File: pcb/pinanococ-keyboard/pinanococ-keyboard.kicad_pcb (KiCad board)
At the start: 2 copper layers, 146.5 x 137.2 mm, 70 parts, among them J1 AudioJack4, SW1 SW_Push, SW10 SW_Push, SW11 SW_Push, SW12 SW_Push, SW14 SW_Push, SW15 SW_Push, SW16 SW_Push, SW17 SW_Push, SW18 SW_Push, SW2 SW_Push, SW20 SW_Push_Dual_x2, SW21 SW_Push, SW22 SW_Push, SW23 SW_Push, SW24 SW_Push, SW26 SW_Push_Dual_x2, SW27 SW_Push, SW28 SW_Push, SW29 SW_Push, SW3 SW_Push, SW30 SW_Push, SW32 SW_Push_Dual_x2, SW33 SW_Push, SW34 SW_Push, SW35 SW_Push, SW36 SW_Push, SW37 SW_Push, SW38 Rotary_Encoder_Switch, SW4 SW_Push, SW5 SW_Push, SW6 SW_Push, SW8 SW_Push, SW9 SW_Push, U1 Pico

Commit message: pcb component layout
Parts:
- added D13: D_ALT, Diode_THT:D_DO-34_SOD68_P7.62mm_Horizontal, F.Cu at (86.2, 134.2)
- SW14: value SW_Push -> SW_Push_Dual_x2; footprint keyswitches:SW_PG1350 -> keyswitches:SW_PG1350_double_rotate
- moved SW14 13.2 mm to (78.0, 124.5)
- moved D14 12.1 mm to (86.2, 124.1)
- moved SW38 5.86 mm to (128.5, 118.8)
- moved U1 5.85 mm to (136.0, 73.0)
- moved e1 5.48 mm to (139.8, 102.0)
- moved D1 5.45 mm to (33.0, 131.2)
- moved D2 5.09 mm to (51.0, 131.1)
- moved D8 5.09 mm to (69.0, 131.1)
- moved D26 4.99 mm to (134.1, 141.2)
- moved D32 4.96 mm to (141.1, 146.6)
- moved SW1 4.70 mm to (24.0, 133.0)
- moved SW2 4.70 mm to (42.0, 133.0)
- moved SW8 4.70 mm to (60.0, 133.0)
- moved SW32 4.40 mm to (146.6, 152.9)
- moved D20 4.33 mm to (111.2, 129.4)
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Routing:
- net ROW_2: track 214.2 -> 0.00 mm
- net COL_0: track 172.7 -> 0.00 mm
- net ROW_3: track 167.2 -> 0.00 mm
- net COL_1: track 160.6 -> 0.00 mm
- net ROW_5: track 142.8 -> 0.00 mm
- net ROW_4: track 141.7 -> 0.00 mm
- net COL_2: track 134.6 -> 0.00 mm
- net COL_3: track 115.0 -> 0.00 mm
- net COL_4: track 101.4 -> 0.00 mm
- net VBUS: track 70.1 -> 0.00 mm
- net COL_5: track 59.7 -> 0.00 mm
- net GND: track 52.9 -> 0.00 mm
- net +3V3: track 49.0 -> 0.00 mm
- net Reset: track 47.8 -> 0.00 mm
- net ROT_B: track 39.6 -> 0.00 mm
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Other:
- board size 146.5 x 137.2 mm -> 146 x 140.8 mm
- net class Default: clearance 0.2 -> 0.254
- rule trace_clearance: 0.2 -> 0.254

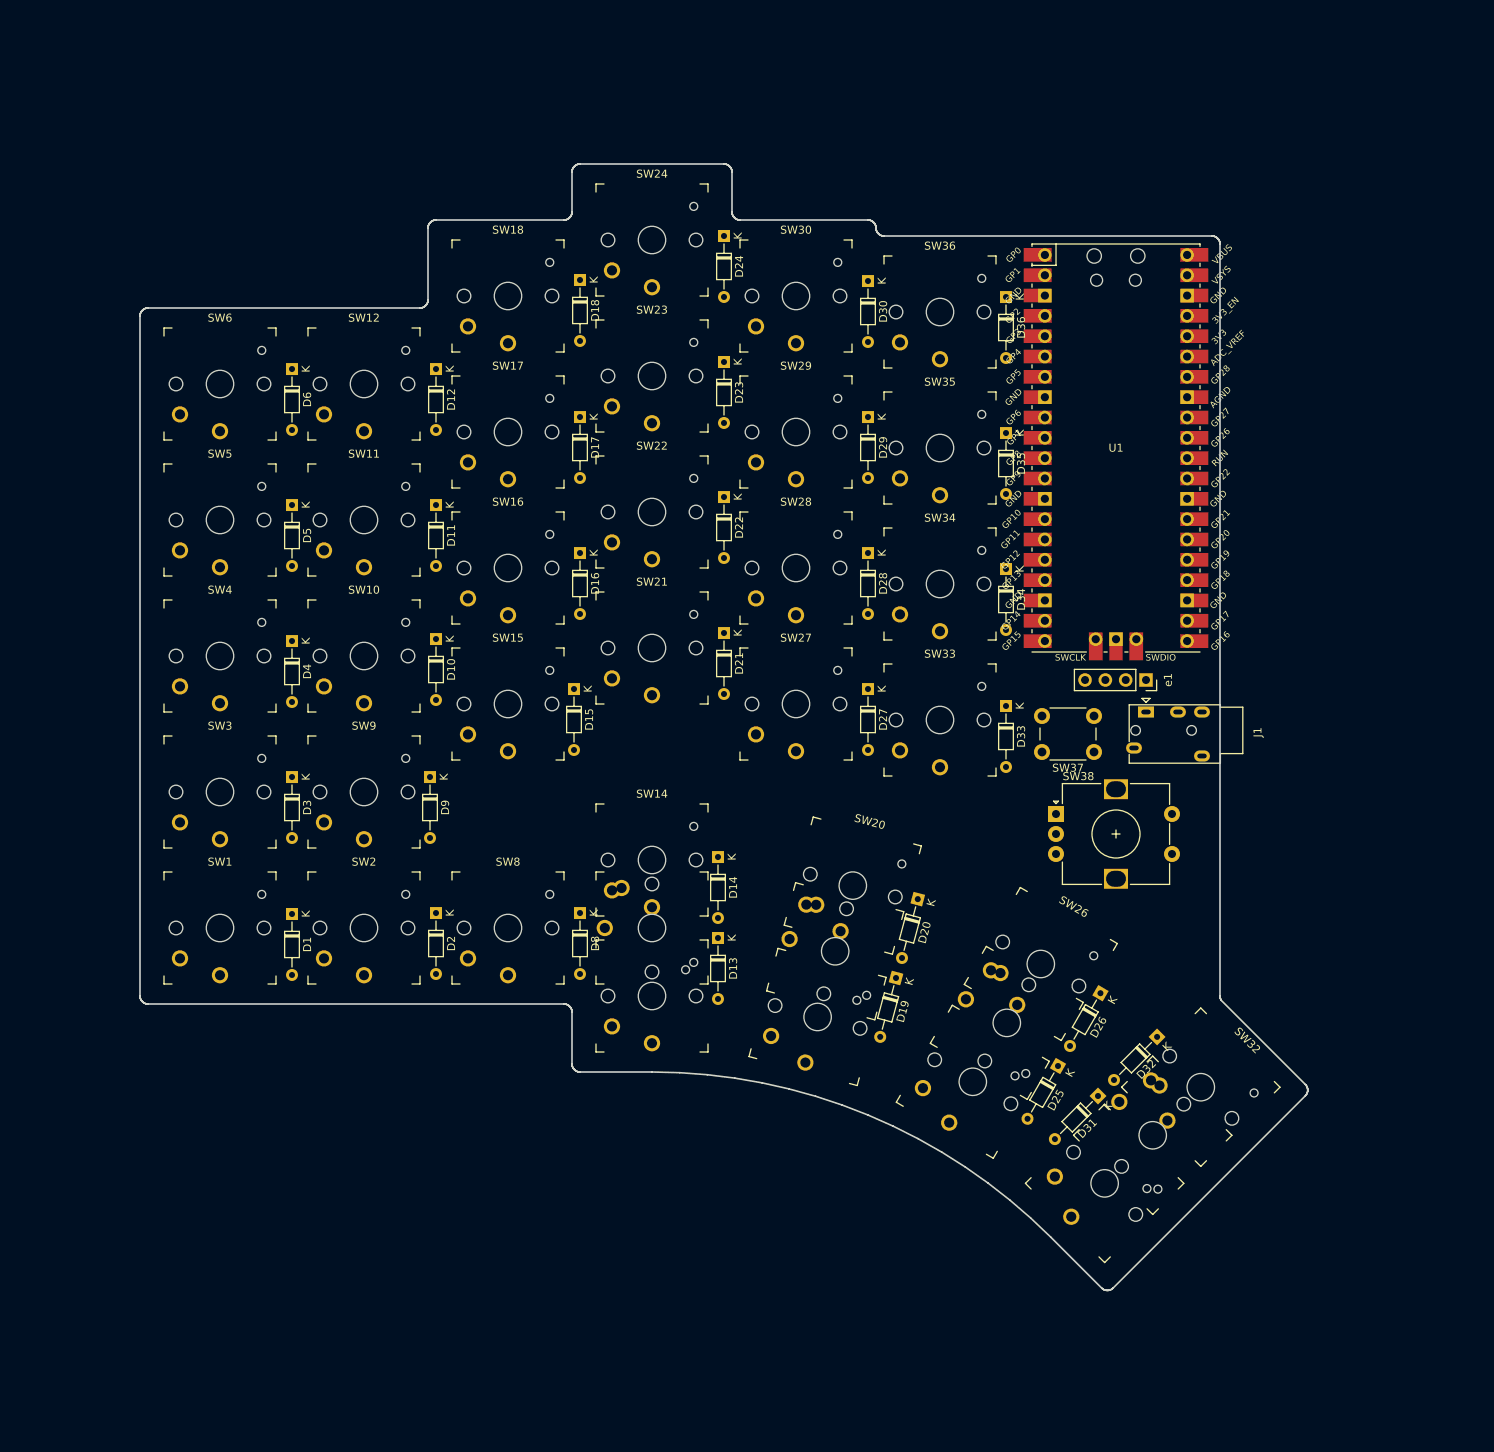
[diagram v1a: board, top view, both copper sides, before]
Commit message: inital pcb layout with tracks
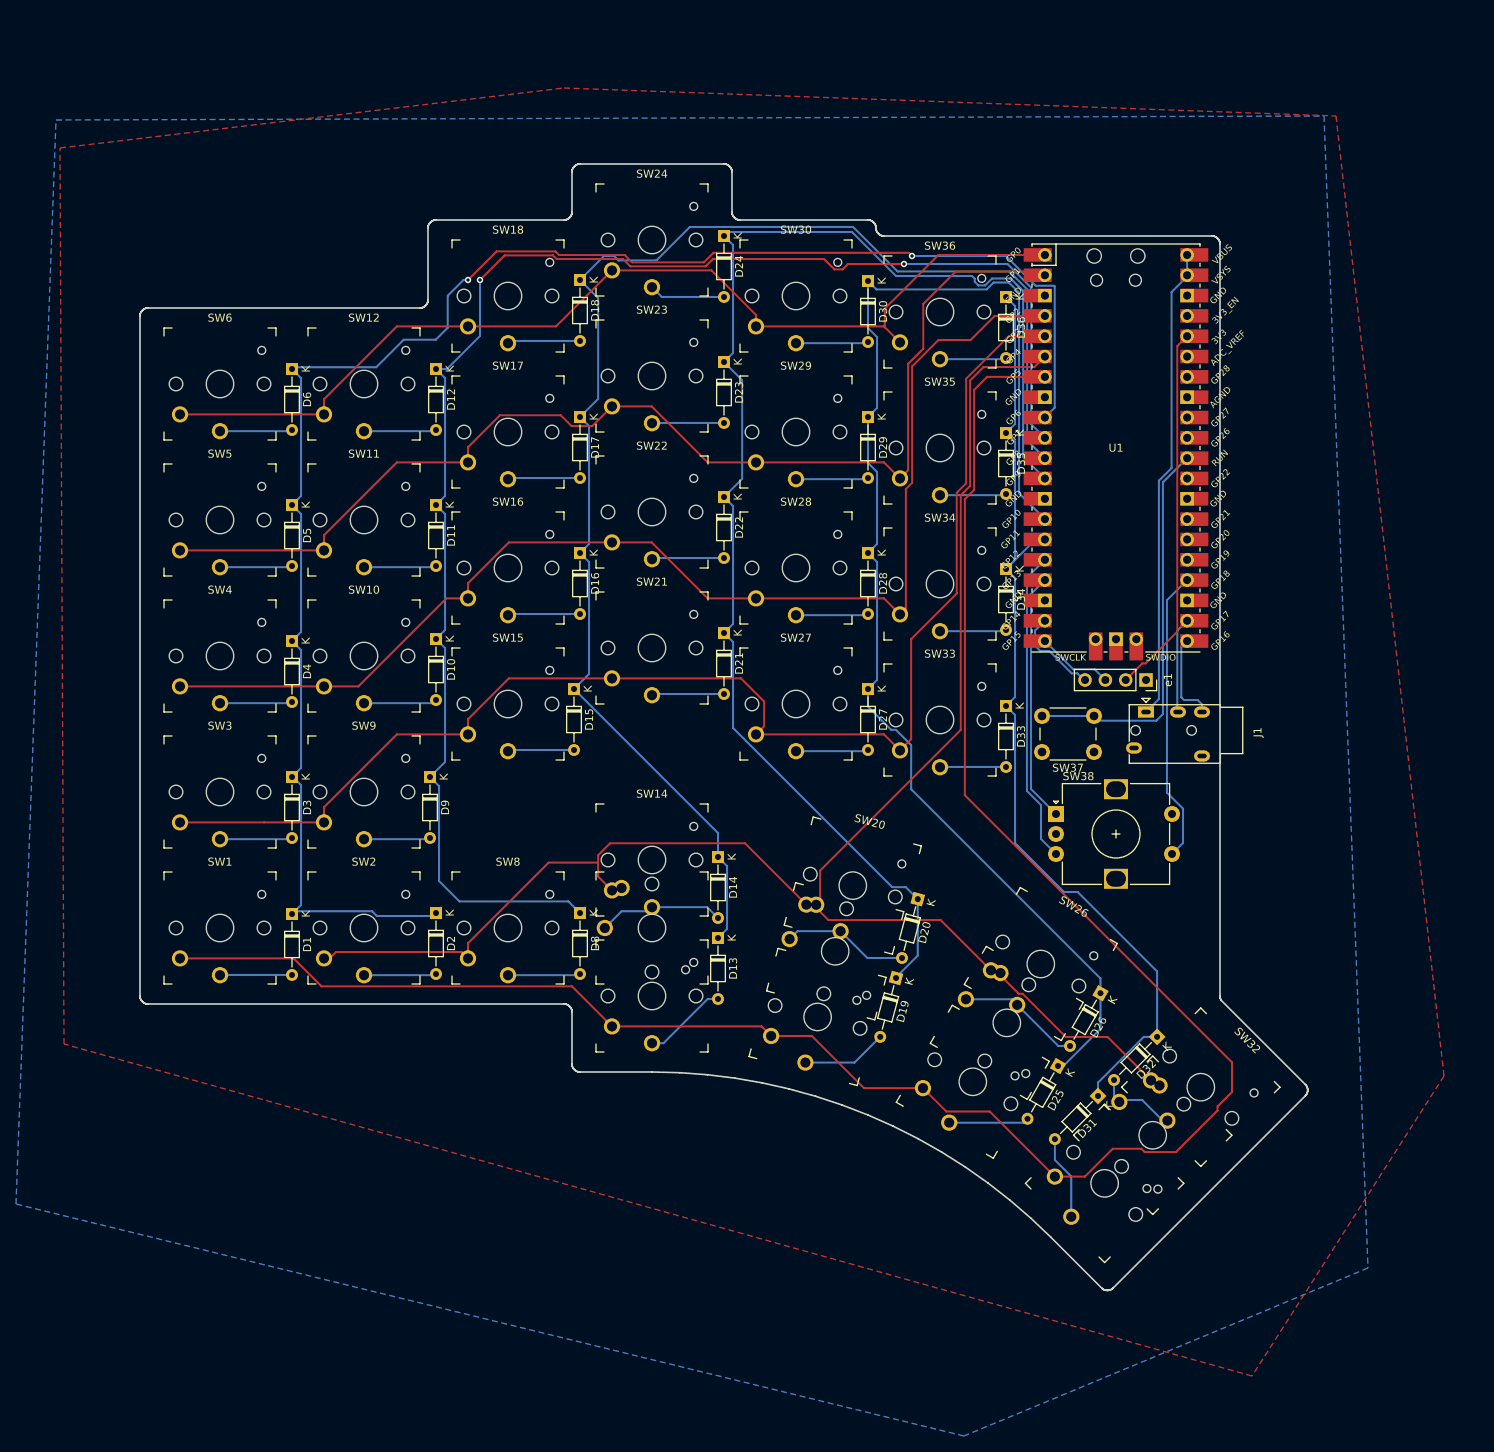
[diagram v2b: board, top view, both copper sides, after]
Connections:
- U1 pad 13: Net-(U1-Pad13) -> GND
- U1 pad 16: ROT_A -> ROT_B
- U1 pad 17: ROT_B -> ROT_A
- U1 pad 18: Net-(U1-Pad18) -> GND
- U1 pad 23: Net-(U1-Pad23) -> GND
- U1 pad 28: Net-(U1-Pad28) -> GND
- U1 pad 3: Net-(U1-Pad3) -> GND
- U1 pad 38: Net-(U1-Pad38) -> GND
- U1 pad 8: Net-(U1-Pad8) -> GND
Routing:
- net ROW_0: track 0.00 -> 259.4 mm
- net ROW_1: track 0.00 -> 215.4 mm
- net COL_0: track 0.00 -> 214.4 mm, vias 0 -> 2
- net COL_1: track 0.00 -> 193.7 mm, vias 0 -> 2
- net COL_2: track 0.00 -> 179.0 mm
- net COL_3: track 0.00 -> 177.3 mm
- net ROW_2: track 0.00 -> 169.2 mm
- net COL_4: track 0.00 -> 165.9 mm
- net ROW_3: track 0.00 -> 153.1 mm
- net ROW_4: track 0.00 -> 144.6 mm
- net ROW_5: track 0.00 -> 128.2 mm
- net COL_5: track 0.00 -> 121.9 mm
- net VBUS: track 0.00 -> 59.3 mm
- net Reset: track 0.00 -> 48.9 mm
- net +3V3: track 0.00 -> 46.4 mm
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- added copper zone on B.Cu, net GND
- added copper zone on F.Cu, net GND

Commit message: inital switch pcb layout
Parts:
- removed D36: D_ALT, Diode_THT:D_DO-34_SOD68_P7.62mm_Horizontal
- removed SW34, SW35, SW36: SW_Push, keyswitches:SW_PG1350
- removed SW37: SW_Push, Button_Switch_THT:SW_PUSH_6mm
- removed SW38: Rotary_Encoder_Switch, Rotary_Encoder:RotaryEncoder_Alps_EC12E-Switch_Vertical_H20mm
- added D7: D_ALT, Diode_THT:D_DO-35_SOD27_P7.62mm_Horizontal, F.Cu at (59.2, 75.0)
- added J2: Conn_02x04_Top_Bottom, Connector_PinHeader_2.54mm:PinHeader_2x04_P2.54mm_Vertical, F.Cu at (140.2, 92.8)
- added J3: Conn_02x02_Top_Bottom, Connector_PinHeader_2.54mm:PinHeader_2x02_P2.54mm_Vertical, F.Cu at (134.0, 90.2)
- added SW13: SW_Push, keyswitches:SW_PG1350_reversible, F.Cu at (68.5, 57.5)
- added SW19: SW_Push, keyswitches:SW_PG1350_reversible, F.Cu at (86.5, 67.5)
- added SW25: SW_Push, keyswitches:SW_PG1350_reversible, F.Cu at (104.5, 91.5)
- added SW31: SW_Push_Dual_x2, footprints:SW_PG1350_reversible_double_rotatable, F.Cu at (155.1, 139.5)
- added SW7: SW_Push, keyswitches:SW_PG1350_reversible, F.Cu at (50.5, 68.5)
- D1, D10, D11, D12, D13, D14, D15, D16, D17, D18, D19, D2, D20, D21, D22, D23, D24, D25, D26, D27, D28, D29, D3, D30, D31, D32, D33, D34, D35, D4, D5, D6, D8, D9: footprint Diode_THT:D_DO-34_SOD68_P7.62mm_Horizontal -> Diode_THT:D_DO-35_SOD27_P7.62mm_Horizontal
- J1: footprint Connector_Audio:Jack_3.5mm_PJ320E_Horizontal -> footprints:TRRS-PJ-320A_reversable
- SW1, SW10, SW11, SW12, SW15, SW17, SW18, SW2, SW22, SW23, SW24, SW27, SW28, SW29, SW3, SW30, SW4, SW5, SW6, SW8, SW9: footprint keyswitches:SW_PG1350 -> keyswitches:SW_PG1350_reversible
- SW14, SW20: value SW_Push_Dual_x2 -> SW_Push; footprint keyswitches:SW_PG1350_double_rotate -> keyswitches:SW_PG1350_reversible
- SW16, SW21: value SW_Push -> SW_Push_Dual_x2; footprint keyswitches:SW_PG1350 -> footprints:SW_PG1350_reversible_double_rotatable
- SW26: footprint keyswitches:SW_PG1350_double_rotate -> footprints:SW_PG1350_reversible_double_rotatable
- SW32: value SW_Push_Dual_x2 -> Rotary_Encoder_Switch; footprint keyswitches:SW_PG1350_double_rotate -> Rotary_Encoder:RotaryEncoder_Alps_EC11E-Switch_Vertical_H20mm
- SW33: footprint keyswitches:SW_PG1350 -> Button_Switch_THT:SW_PUSH_6mm
- U1: footprint MCU_RaspberryPi_and_Boards:RPi_Pico_SMD_TH -> footprints:RPi_Pico_SMD_TH_flipable
- e1: footprint Connector_PinSocket_2.54mm:PinSocket_1x04_P2.54mm_Vertical -> Connector_PinHeader_2.54mm:PinHeader_1x04_P2.54mm_Vertical
- moved D25 87.5 mm to (113.8, 64.0), turned to 90 degrees
- moved D31 86.1 mm to (129.0, 68.0), turned to 180 degrees
- moved D19 83.3 mm to (95.5, 57.0), turned to 90 degrees
- moved SW1 81.9 mm to (32.5, 51.5)
- moved D29 80.4 mm to (134.2, 144.0), turned to 52.5 degrees
- moved D23 78.0 mm to (117.0, 134.2), turned to 67.5 degrees
- moved D35 75.7 mm to (136.2, 145.5), turned to 52.5 degrees
- moved D1 73.7 mm to (41.5, 58.0), turned to 90 degrees
- moved D13 70.8 mm to (77.5, 64.0), turned to 90 degrees
- moved SW27 67.9 mm to (122.5, 42.5)
- moved D26 67.7 mm to (113.5, 76.6), turned to 90 degrees
- moved D17 66.1 mm to (97.0, 129.0), turned to 82.5 degrees
- moved SW2 65.2 mm to (32.5, 68.5)
- moved D32 62.8 mm to (129.0, 85.0), turned to 180 degrees
- moved D28 60.3 mm to (142.2, 133.5), turned to 52.5 degrees
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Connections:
- D12 pad 1: COL_1 -> COL_2
- D18 pad 1: COL_2 -> COL_3
- D24 pad 1: COL_3 -> COL_4
- D30 pad 1: COL_4 -> COL_5
- D6 pad 1: COL_0 -> COL_1
- SW1 pad 2: ROW_0 -> ROW_5
- SW10 pad 2: ROW_3 -> ROW_1
- SW11 pad 2: ROW_4 -> ROW_0
- SW14 pad 2: ROW_1 -> ROW_3
- SW16 pad 2: ROW_3 -> ROW_1
- SW17 pad 1: Net-(D17-Pad2) -> Net-(D18-Pad2)
- SW17 pad 2: ROW_4 -> ROW_5
- SW18 pad 1: Net-(D18-Pad2) -> Net-(D19-Pad2)
- SW18 pad 2: ROW_5 -> ROW_4
- SW2 pad 2: ROW_1 -> ROW_4
- SW20 pad 1: Net-(D20-Pad2) -> Net-(D21-Pad2)
- SW20 pad 2: ROW_1 -> ROW_2
- SW21 pad 1: Net-(D21-Pad2) -> Net-(D22-Pad2)
- SW21 pad 2: ROW_2 -> ROW_1
- SW22 pad 1: Net-(D22-Pad2) -> Net-(D24-Pad2)
- SW22 pad 2: ROW_3 -> ROW_5
- SW23 pad 1: Net-(D23-Pad2) -> Net-(D25-Pad2)
- SW24 pad 1: Net-(D24-Pad2) -> Net-(D26-Pad2)
- SW24 pad 2: ROW_5 -> ROW_3
- SW26 pad 1: Net-(D26-Pad2) -> Net-(D28-Pad2)
- SW26 pad 3: Net-(D25-Pad2) -> Net-(D29-Pad2)
- SW27 pad 1: Net-(D27-Pad2) -> Net-(D30-Pad2)
- SW27 pad 2: ROW_2 -> ROW_5
- SW28 pad 1: Net-(D28-Pad2) -> Net-(D31-Pad2)
- SW28 pad 2: ROW_3 -> ROW_4
- SW29 pad 1: Net-(D29-Pad2) -> Net-(D32-Pad2)
- SW29 pad 2: ROW_4 -> ROW_3
- SW3 pad 2: ROW_2 -> ROW_3
- SW30 pad 1: Net-(D30-Pad2) -> Net-(D33-Pad2)
- SW30 pad 2: ROW_5 -> ROW_2
- SW33 pad 1: Net-(D33-Pad2) -> GND
- SW33 pad 2: ROW_2 -> Reset
- SW4 pad 2: ROW_3 -> ROW_2
- SW5 pad 2: ROW_4 -> ROW_1
- SW8 pad 2: ROW_1 -> ROW_3
- U1 pad 1: ROW_5 -> VBUS
- U1 pad 10: COL_1 -> ROW_3
- U1 pad 11: COL_2 -> Net-(J3-Pad2)
- U1 pad 12: COL_3 -> ROW_2
- U1 pad 14: COL_4 -> ROW_1
- U1 pad 15: COL_5 -> ROW_0
- U1 pad 16: ROT_B -> UART_TX
- U1 pad 17: ROT_A -> UART_RX
- U1 pad 19: I2C_SDA -> I2C_SCL_SDA
- U1 pad 2: ROW_4 -> VBUS
- U1 pad 20: I2C_SCL -> I2C_SDA_SCL
- U1 pad 21: UART_TX -> ROT_A
- U1 pad 22: UART_RX -> ROT_B
- U1 pad 24: ROT_SW -> UART_TX
- U1 pad 25: Net-(U1-Pad25) -> UART_RX
- U1 pad 26: Net-(U1-Pad26) -> COL_0
- U1 pad 27: Net-(U1-Pad27) -> COL_1
- U1 pad 29: Net-(U1-Pad29) -> COL_2
- U1 pad 30: Reset -> Net-(J3-Pad1)
- U1 pad 31: Net-(U1-Pad31) -> COL_3
- U1 pad 32: Net-(U1-Pad32) -> COL_4
- U1 pad 33: Net-(U1-Pad33) -> GND
- U1 pad 34: Net-(U1-Pad34) -> COL_5
- U1 pad 4: ROW_3 -> Net-(U1-Pad4)
- U1 pad 5: ROW_2 -> +3V3
- U1 pad 6: ROW_1 -> Net-(U1-Pad6)
- U1 pad 7: ROW_0 -> ROW_5
- U1 pad 9: COL_0 -> ROW_4
- e1 pad 1: GND -> Net-(J2-Pad2)
- e1 pad 2: +3V3 -> Net-(J2-Pad4)
- e1 pad 3: I2C_SCL -> Net-(J2-Pad6)
- e1 pad 4: I2C_SDA -> Net-(J2-Pad8)
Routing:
- net ROW_0: track 259.4 -> 0.00 mm
- net ROW_1: track 215.4 -> 0.00 mm
- net COL_0: track 214.4 -> 0.00 mm, vias 2 -> 0
- net COL_1: track 193.7 -> 0.00 mm, vias 2 -> 0
- net COL_2: track 179.0 -> 0.00 mm
- net COL_3: track 177.3 -> 0.00 mm
- net ROW_2: track 169.2 -> 0.00 mm
- net COL_4: track 165.9 -> 0.00 mm
- net ROW_3: track 153.1 -> 0.00 mm
- net ROW_4: track 144.6 -> 0.00 mm
- net ROW_5: track 128.2 -> 0.00 mm
- net COL_5: track 121.9 -> 0.00 mm
- net VBUS: track 59.3 -> 0.00 mm
- net Reset: track 48.9 -> 0.00 mm
- net +3V3: track 46.4 -> 0.00 mm
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- removed copper zone on B.Cu, net GND
- removed copper zone on F.Cu, net GND

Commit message: first pass tracks for pcb
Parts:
- moved D14 0.25 mm to (77.5, 80.8)
- moved D15 0.25 mm to (75.0, 83.0)
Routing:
- net ROW_1: track 0.00 -> 290.1 mm
- net ROW_0: track 0.00 -> 192.6 mm
- net COL_1: track 0.00 -> 190.8 mm
- net COL_0: track 0.00 -> 189.7 mm
- net COL_4: track 0.00 -> 188.9 mm
- net GND: track 0.00 -> 188.6 mm
- net COL_2: track 0.00 -> 182.9 mm
- net COL_5: track 0.00 -> 181.7 mm
- net ROW_2: track 0.00 -> 177.7 mm
- net COL_3: track 0.00 -> 170.5 mm
- net ROW_4: track 0.00 -> 157.4 mm
- net ROW_3: track 0.00 -> 157.3 mm
- net ROW_5: track 0.00 -> 139.0 mm
- net VBUS: track 0.00 -> 112.1 mm
- net UART_TX: track 0.00 -> 91.5 mm
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
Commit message: v0.1 pcb layout
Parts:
- added REF**: OSHW-Logo2_9.8x8mm_SilkScreen, Symbol:OSHW-Logo2_9.8x8mm_SilkScreen, B.Cu at (86.5, 97.8)
- added REF**: OSHW-Logo2_9.8x8mm_SilkScreen, Symbol:OSHW-Logo2_9.8x8mm_SilkScreen, F.Cu at (86.5, 97.8)
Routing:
- net ROW_1: track 290.1 -> 308.2 mm
- net COL_4: track 188.9 -> 201.6 mm
- net COL_5: track 181.7 -> 191.7 mm
- net COL_0: track 189.7 -> 195.4 mm
- net COL_2: track 182.9 -> 186.5 mm
- net ROW_4: track 157.4 -> 161.0 mm
- net COL_1: track 190.8 -> 194.2 mm
- net ROW_3: track 157.3 -> 160.2 mm
- net ROW_0: track 192.6 -> 189.9 mm
- net COL_3: track 170.5 -> 173.0 mm
- net Net-(D12-Pad2): track 13.3 -> 11.9 mm
- net Net-(D14-Pad2): track 13.3 -> 12.0 mm
- net UART_TX: track 91.5 -> 92.6 mm
- net Net-(D34-Pad2): track 23.8 -> 24.9 mm
- net Net-(D22-Pad2): track 23.6 -> 24.2 mm
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- added copper zone on B.Cu, net GND
- added copper zone on F.Cu, net GND
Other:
- board text added: "JLCJLCJLCJLC"
- board text added: "pinacochoc v0.1 @DLKJ"
